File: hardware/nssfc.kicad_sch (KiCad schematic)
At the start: 0 parts

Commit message: made the schematic
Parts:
- added C1, C2: 2.2u, symbol Device:C
- added C10: 1u, symbol Device:C_Small
- added C11: 4.7u, symbol Device:C
- added C12, C5, C6, C7, C8, C9: 100n, symbol Device:C_Small
- added C3, C4: 15p, symbol Device:C_Small
- added R1: 10k, symbol Device:R_Small_US
- added TP1, TP2: TestPoint, symbol Connector:TestPoint
- added U1: STM32F405RGTx, Package_QFP:LQFP-64_10x10mm_P0.5mm, symbol MCU_ST_STM32F4:STM32F405RGTx
- added U2: W25Q128JVP, Package_SON:WSON-8-1EP_6x5mm_P1.27mm_EP3.4x4.3mm, symbol Memory_Flash:W25Q128JVP
- added U3: QMC5883P, nssfc:LGA-16_3x3_Pitch0.5mm_QMC5883P, symbol nssfc:QMC5883P
- added U4: ICM-20602, Package_LGA:LGA-16_3x3mm_P0.5mm_LayoutBorder3x5y, symbol Sensor_Motion:ICM-20602
- added U5: BMP580, Package_LGA:ST_HLGA-10_2x2mm_P0.5mm_LayoutBorder3x2y, symbol nssfc:BMP580
- added Y1: 25MHz, symbol Device:Crystal_GND24
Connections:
- new net: C2.1, U1.31 (VCAP_1)
- new net: C1.1, U1.47 (VCAP_2)
- new net: C11.1, U3.10 (C1)
- new net: U5.3 (VSS), U5.8 (VSS), U5.9 (VSS)
- new net: U3.12 (NC), U3.13 (NC), U3.14 (NC), U3.15 (NC), U3.3 (NC), U3.4 (NC), U3.5 (NC), U3.6 (NC), U3.7 (NC), U3.8 (NC)
- new net +3V3: C10.1, C12.1, C5.1, C6.1, C7.1, C8.1, C9.1, R1.1, U1.1 (VBAT), U1.13 (VDDA), U1.19 (VDD), U1.32 (VDD), U1.48 (VDD), U1.64 (VDD), U2.8 (VCC)
- new net F_SPI_CLK: U2.6 (CLK)
- new net F_SPI_MISO: U2.2 (DO/IO_{1})
- new net F_SPI_MOSI: U2.5 (DI/IO_{0})
- new net GND: C1.2, C10.2, C11.2, C12.2, C2.2, C3.2, C4.2, C5.2, C6.2, C7.2, C8.2, C9.2, TP1.1, U1.12 (VSSA), U1.18 (VSS), U1.63 (VSS), U2.4 (GND), U2.9 (EP), U3.11 (GND), U3.9 (GND), U4.10 (GND), U4.11 (GND), U4.12 (GND), U4.13 (GND), U4.15 (GND), U4.9 (GND), Y1.2 (G), Y1.4 (G)
- new net M_SCK: U3.1 (SCK)
- new net M_SDA: U3.16 (SDA)
- new net NRST: R1.2, TP2.1, U1.7 (NRST)
- new net PH0: C3.1, U1.5 (PH0), Y1.1
- new net PH1: C4.1, U1.6 (PH1), Y1.3
- new net ~{F_SPI_CS}: U2.1 (~{CS})
- new net ~{F_SPI_RST}: U2.7 (~{HOLD}/~{RESET}/IO_{3})
- new net ~{F_SPI_WP}: U2.3 (~{WP}/IO_{2})
- no-connect marks 0 -> 1
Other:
- note added: "15pF capacitance taken assuming 10pF crystal load capacitance and 2.5pF stray capacitance."
- note added: "Barometer"
- note added: "Crystal"
- note added: "Flash"
- note added: "IMU"
- note added: "Magnetometer"
- note added: "add appropriate power converters"
- note added: "button to be added here"
- note added: "ensure ESR<200m (thus no 0402)"
- note added: "qSPI mode not used because stm32f405 does not support it."
- note added: "use SPI with the IMU"

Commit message: saving the repository
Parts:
- added C13, C14: 100n, symbol Device:C_Small
- added C15, C16: .1u, symbol Device:C_Small
- added C17: 2.2u, symbol Device:C_Small
- added C18: 10n, symbol Device:C_Small
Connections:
- net +3V3: now also U4.16 (VDD), C16.1, C17.1
- net GND: now also U5.3 (VSS), U5.8 (VSS), U5.9 (VSS), C13.1, C14.1, C15.2, C16.2, C17.2, C18.1
- net BMP_SPI_MISO: now reaches U1.10 (PC2)
- net BMP_SPI_MISO: now also U5.5 (SDO)
- net BMP_SPI_MOSI: now reaches U1.11 (PC3)
- net BMP_SPI_MOSI: now also U5.4 (SDI)
- net IMU_SPI_CS: now reaches U1.20 (PA4)
- net IMU_SPI_CS: now also U4.5 (~{CS})
- net IMU_SPI_SCK: now reaches U1.21 (PA5)
- net IMU_SPI_SCK: now also U4.2 (SCL/SPC)
- net IMU_SPI_MISO: now reaches U1.22 (PA6)
- net IMU_SPI_MISO: now also U4.4 (SAO/SD0)
- net IMU_SPI_MOSI: now reaches U1.23 (PA7)
- net IMU_SPI_MOSI: now also U4.3 (SDA/SDI)
- net BMP_SPI_SCK: now reaches U1.29 (PB10)
- net BMP_SPI_SCK: now also U5.2 (SCK)
- net BMP_SPI_CSB: now reaches U1.33 (PB12)
- net BMP_SPI_CSB: now also U5.6 (CSB)
- net at U5.1 (VDDIO): now also C13.2
- net at U5.10 (VDD): now also C14.2
- net at U4.1 (VDDIO): now also C18.2
- net at U4.14 (REGOUT): now also C15.1
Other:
- moved on the sheet: U4

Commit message: worked on the schematic
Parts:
- added C19, C23, C25: 100n, Capacitor_SMD:C_0402_1005Metric, symbol Device:C_Small
- added C20: 22u, Capacitor_SMD:C_0805_2012Metric, symbol Device:C
- added C21, C22, C24: 10u, Capacitor_SMD:C_0805_2012Metric, symbol Device:C
- added D1, D2: D_Schottky, Diode_SMD:D_SOD-123F, symbol Device:D_Schottky_Small
- added J1: USB_C_Receptacle_USB2.0_16P, Connector_USB:USB_C_Receptacle_XKB_U262-16XN-4BVC11, symbol Connector:USB_C_Receptacle_USB2.0_16P
- added L1: 4.7u, Inductor_SMD:L_Changjiang_FNR4020S, symbol Device:L
- added R2, R3: 4.7k, Resistor_SMD:R_0402_1005Metric, symbol Device:R_Small_US
- added R4, R5: 5.1k, Resistor_SMD:R_0402_1005Metric, symbol Device:R_Small_US
- added R6: 10k, Resistor_SMD:R_0402_1005Metric, symbol Device:R_Small_US
- added SW1: SW_Push, Button_Switch_SMD:SW_SPST_PTS810, symbol Switch:SW_Push
- added U6: AP63205WU, Package_TO_SOT_SMD:TSOT-23-6, symbol Regulator_Switching:AP63205WU
- added U7: TLV75733PDBV, Package_TO_SOT_SMD:SOT-23-5, symbol Regulator_Linear:TLV75733PDBV
- C1, C10, C12, C13, C14, C18, C2, C3, C4, C5, C6, C7, C8, C9: footprint (none) -> Capacitor_SMD:C_0402_1005Metric
- C11: footprint (none) -> Capacitor_SMD:C_0805_2012Metric
- C15: value .1u -> 100n; footprint (none) -> Capacitor_SMD:C_0402_1005Metric
- C16: value .1u -> 2.2u; footprint (none) -> Capacitor_SMD:C_0402_1005Metric
- C17: value 2.2u -> 100n; footprint (none) -> Capacitor_SMD:C_0402_1005Metric
- R1: footprint (none) -> Resistor_SMD:R_0402_1005Metric
- TP1, TP2: footprint (none) -> TestPoint:TestPoint_Pad_1.0x1.0mm
- Y1: footprint (none) -> Crystal:Crystal_SMD_3225-4Pin_3.2x2.5mm
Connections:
- net +3V3: now also C13.1, C14.1, C18.1, U3.2 (VDD), U4.1 (VDDIO), U5.1 (VDDIO), U5.10 (VDD), C24.1, C25.1, R2.1, R3.1, SW1.1, U7.5 (OUT)
- net BMP_SPI_MISO: now also U1.35 (PB14); no longer U1.10 (PC2)
- net BMP_SPI_MOSI: now also U1.36 (PB15); no longer U1.11 (PC3)
- net BMP_SPI_SCK: now also U1.34 (PB13); no longer U1.29 (PB10)
- net F_SPI_CLK: now also U1.51 (PC10)
- net F_SPI_MISO: now also U1.52 (PC11)
- net F_SPI_MOSI: now also U1.53 (PC12)
- net GND: now also C13.2, C14.2, C18.2, C20.2, C21.2, C22.2, C23.2, C24.2, C25.2, J1.A1 (GND), J1.A12 (GND), J1.B1 (GND), J1.B12 (GND), J1.SH (SHIELD), R4.2, R5.2, R6.2, U6.4 (GND), U7.2 (GND); no longer C13.1, C14.1, C18.1
- net M_SCK: now also U1.59 (PB7), R3.2
- net M_SDA: now also U1.58 (PB6), R2.2
- net ~{F_SPI_CS}: now also U1.50 (PA15)
- net ~{F_SPI_RST}: now also U1.49 (PA14)
- net ~{F_SPI_WP}: now also U1.46 (PA13)
- net IMU_SPI_INT: now reaches U1.17 (PA3)
- net IMU_SPI_INT: now also U4.6 (INT)
- net BMP_SPI_INT: now reaches U1.30 (PB11)
- net BMP_SPI_INT: now also U5.7 (INT)
- net USB_DN: now reaches U1.44 (PA11)
- net USB_DN: now also J1.A7 (D-), J1.B7 (D-)
- net USB_DP: now reaches U1.45 (PA12)
- net USB_DP: now also J1.A6 (D+), J1.B6 (D+)
- net at U1.60 (BOOT0): now also R6.1, SW1.2
- new net: D1.2 (A), J1.A4 (VBUS), J1.A9 (VBUS), J1.B4 (VBUS), J1.B9 (VBUS)
- new net: J1.A5 (CC1), R5.1
- new net: J1.B5 (CC2), R4.1
- new net: C20.1, D2.2 (A), L1.2, U6.1 (FB)
- new net: C19.1, L1.1, U6.5 (SW)
- new net: C19.2, U6.6 (BST)
- new net +5V: C22.1, C23.1, D1.1 (K), D2.1 (K), U7.1 (IN), U7.3 (EN)
- new net VBUS: C21.1, U6.2 (EN), U6.3 (IN)
- no-connect marks 1 -> 3
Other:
- note added: "V_batt to 5v"
- note added: "add 9v buck boost"
- note added: "add power LEDs add connection pads add UARTS and I2C and SBUS controls"
- note added: "buck converter"
- note added: "main LDO"
- note removed: "add appropriate power converters"
- note removed: "button to be added here"
- moved on the sheet: C1, C10, C11, C12, C15, C2, C3, C4, C5, C6, C7, C8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

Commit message: worked on PCB layout
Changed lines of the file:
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@@
+	)
+	(junction
+		(at 213.36 102.87)
+		(diameter 0)
+		(color 0 0 0 0)
+	)
+	(junction
+		(at 261.62 49.53)
+		(diameter 0)
+		(color 0 0 0 0)
+	)
+	(junction
+		(at 276.86 49.53)
+		(diameter 0)
+		(color 0 0 0 0)
+	)
+	(junction
+		(at 236.22 50.8)
+		(diameter 0)
+		(color 0 0 0 0)
+	)
+	(junction
+		(at 82.55 116.84)
+		(diameter 0)
+		(color 0 0 0 0)
+	)
+	(junction
+		(at 212.09 184.15)
+		(diameter 0)
+		(color 0 0 0 0)
+	)
+	(junction
+		(at 60.96 113.03)
+		(diameter 0)
+		(color 0 0 0 0)
+	)
+	(junction
+		(at 269.24 134.62)
+		(diameter 0)
+		(color 0 0 0 0)
+	)
+	(junction
+		(at 62.23 85.09)
+		(diameter 0)
+		(color 0 0 0 0)
+	)
+	(junction
+		(at 201.93 50.8)
+		(diameter 0)
+		(color 0 0 0 0)
+	)
+	(junction
+		(at 168.91 49.53)
+		(diameter 0)
+		(color 0 0 0 0)
+	)
+	(junction
+		(at 146.05 128.27)
+		(diameter 0)
+		(color 0 0 0 0)
+	)
+	(junction
+		(at 161.29 49.53)
+		(diameter 0)
+		(color 0 0 0 0)
+	)
+	(junction
+		(at 180.34 115.57)
+		(diameter 0)
+		(color 0 0 0 0)
 	)
 	(junction
@@
 	)
 	(junction
-		(at 213.36 102.87)
-		(diameter 0)
-		(color 0 0 0 0)
-	)
-	(junction
-		(at 261.62 49.53)
-		(diameter 0)
-		(color 0 0 0 0)
-	)
-	(junction
-		(at 276.86 49.53)
-		(diameter 0)
-		(color 0 0 0 0)
-	)
-	(junction
-		(at 236.22 50.8)
-		(diameter 0)
-		(color 0 0 0 0)
-	)
-	(junction
-		(at 82.55 116.84)
-		(diameter 0)
-		(color 0 0 0 0)
-	)
-	(junction
-		(at 60.96 113.03)
-		(diameter 0)
-		(color 0 0 0 0)
-	)
-	(junction
-		(at 269.24 134.62)
-		(diameter 0)
-		(color 0 0 0 0)
-	)
-	(junction
-		(at 62.23 85.09)
-		(diameter 0)
-		(color 0 0 0 0)
-	)
-	(junction
-		(at 201.93 50.8)
-		(diameter 0)
-		(color 0 0 0 0)
-	)
-	(junction
-		(at 168.91 49.53)
-		(diameter 0)
-		(color 0 0 0 0)
-	)
-	(junction
-		(at 146.05 128.27)
-		(diameter 0)
-		(color 0 0 0 0)
-	)
-	(junction
-		(at 161.29 49.53)
-		(diameter 0)
-		(color 0 0 0 0)
-	)
-	(junction
-		(at 180.34 115.57)
-		(diameter 0)
-		(color 0 0 0 0)
-	)
-	(junction
 		(at 81.28 64.77)
 		(diameter 0)
@@
 	(junction
 		(at 217.17 175.26)
-		(diameter 0)
-		(color 0 0 0 0)
-	)
-	(junction
-		(at 212.09 184.15)
 		(diameter 0)
 		(color 0 0 0 0)
@@
 	(wire
 		(pts
-			(xy 212.09 184.15) (xy 232.41 184.15)
+			(xy 212.09 184.15) (xy 234.95 184.15)
 		)
 		(stroke
@@
 	(wire
 		(pts
-			(xy 222.25 181.61) (xy 232.41 181.61)
+			(xy 222.25 181.61) (xy 234.95 181.61)
 		)
 		(stroke
@@
 	)
 	(label "M_SCK"
-		(at 232.41 184.15 180)
+		(at 234.95 184.15 180)
 		(effects
 			(font
@@
 	)
 	(label "M_SDA"
-		(at 232.41 181.61 180)
+		(at 234.95 181.61 180)
 		(effects
 			(font

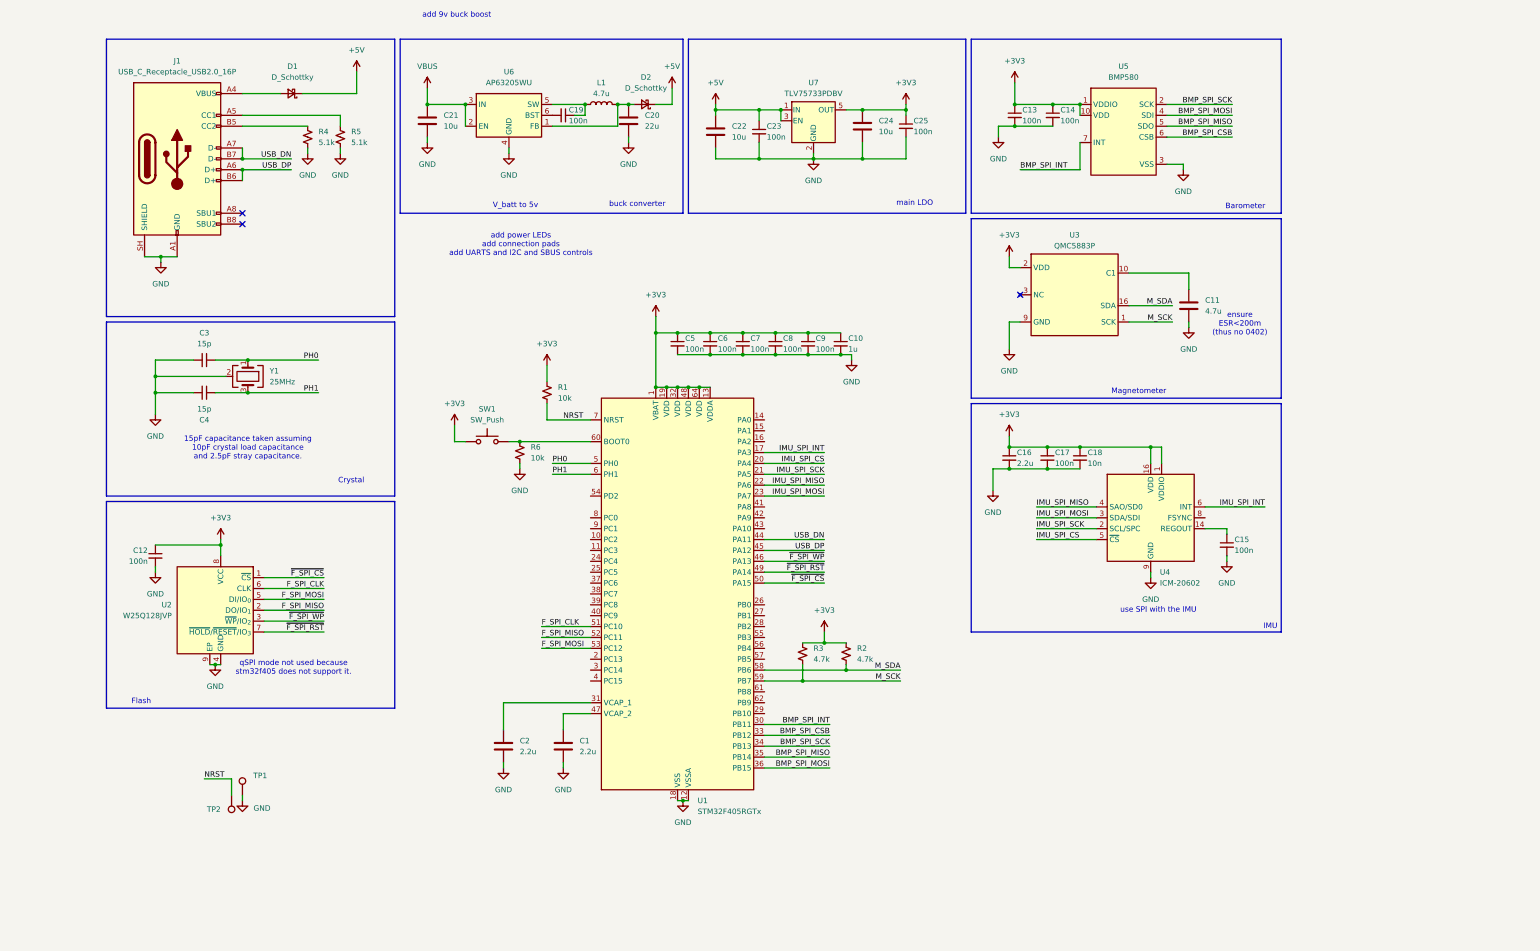
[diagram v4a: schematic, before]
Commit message: layout change in PCB
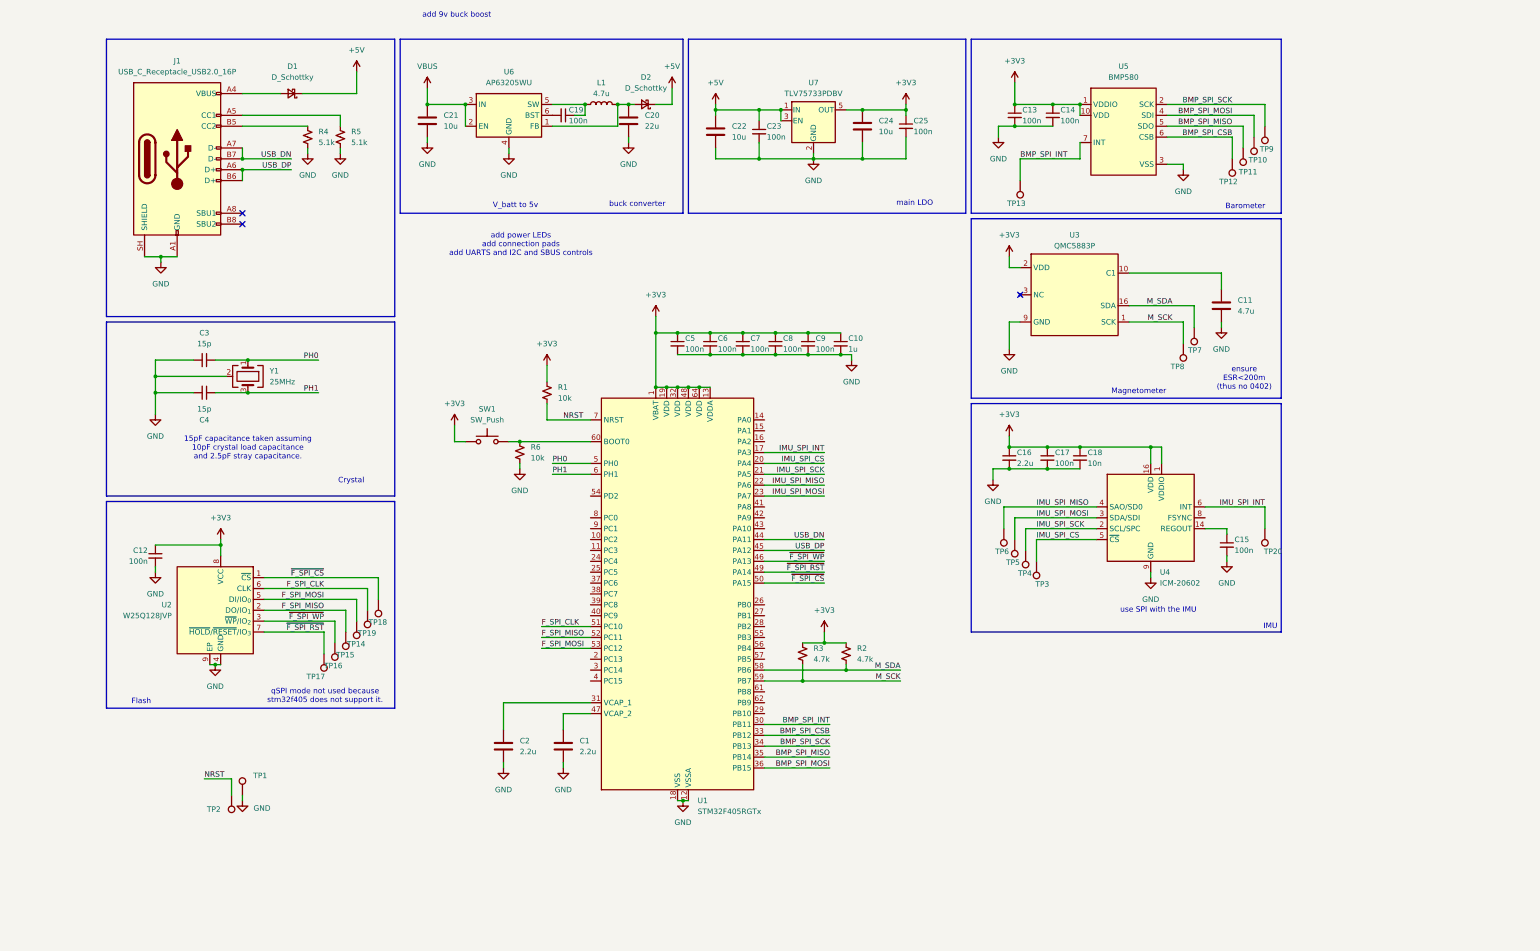
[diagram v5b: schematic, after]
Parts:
- added TP10, TP11, TP12, TP13, TP14, TP15, TP16, TP17, TP18, TP19, TP20, TP3, TP4, TP5, TP6, TP7, TP8, TP9: TestPoint, TestPoint:TestPoint_Pad_1.5x1.5mm, symbol Connector:TestPoint
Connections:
- net BMP_SPI_CSB: now also TP12.1
- net BMP_SPI_INT: now also TP13.1
- net BMP_SPI_MISO: now also TP11.1
- net BMP_SPI_MOSI: now also TP10.1
- net BMP_SPI_SCK: now also TP9.1
- net F_SPI_CLK: now also TP19.1
- net F_SPI_MISO: now also TP15.1
- net F_SPI_MOSI: now also TP14.1
- net IMU_SPI_CS: now also TP3.1
- net IMU_SPI_INT: now also TP20.1
- net IMU_SPI_MISO: now also TP6.1
- net IMU_SPI_MOSI: now also TP5.1
- net IMU_SPI_SCK: now also TP4.1
- net M_SCK: now also TP8.1
- net M_SDA: now also TP7.1
- net ~{F_SPI_CS}: now also TP18.1
- net ~{F_SPI_RST}: now also TP17.1
- net ~{F_SPI_WP}: now also TP16.1
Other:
- moved on the sheet: C11

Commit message: placement session: i am locked in
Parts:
- added D3, D4, D5: LED, LED_SMD:LED_0402_1005Metric, symbol Device:LED
- added R7: 1k, Resistor_SMD:R_0402_1005Metric, symbol Device:R_Small_US
- added R8: 220, Resistor_SMD:R_0402_1005Metric, symbol Device:R_Small_US
- added R9: 100, Resistor_SMD:R_0402_1005Metric, symbol Device:R_Small_US
- added TP21, TP22, TP23, TP24, TP25, TP26, TP27, TP28, TP29, TP30, TP31, TP32, TP33, TP34, TP35, TP36, TP37, TP38, TP39, TP40, TP41, TP42, TP43, TP44, TP45, TP46, TP47, TP48, TP49: TestPoint, nssfc:PAD_1.5mm, symbol Connector:TestPoint
- added TP50, TP51: TestPoint, TestPoint:TestPoint_Pad_3.0x3.0mm, symbol Connector:TestPoint
- TP10, TP11, TP12, TP13, TP14, TP15, TP16, TP17, TP18, TP19, TP20, TP3, TP4, TP5, TP6, TP7, TP8, TP9: footprint TestPoint:TestPoint_Pad_1.5x1.5mm -> nssfc:PAD_1.5mm
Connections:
- net +3V3: now also D5.2 (A)
- net +5V: now also D4.2 (A)
- net GND: now also R7.2, R8.2, R9.2, TP51.1
- net VBUS: now also D3.2 (A), TP50.1
- net at U1.10 (PC2): now also TP23.1
- net at U1.11 (PC3): now also TP24.1
- net at U1.14 (PA0): now also TP35.1
- net at U1.15 (PA1): now also TP36.1
- net at U1.16 (PA2): now also TP37.1
- net at U1.2 (PC13): now also TP31.1
- net at U1.24 (PC4): now also TP25.1
- net at U1.25 (PC5): now also TP26.1
- net at U1.26 (PB0): now also TP41.1
- net at U1.27 (PB1): now also TP42.1
- net at U1.28 (PB2): now also TP43.1
- net at U1.29 (PB10): now also TP49.1
- net at U1.3 (PC14): now also TP32.1
- net at U1.37 (PC6): now also TP27.1
- net at U1.38 (PC7): now also TP28.1
- net at U1.39 (PC8): now also TP29.1
- net at U1.4 (PC15): now also TP33.1
- net at U1.40 (PC9): now also TP30.1
- net at U1.41 (PA8): now also TP38.1
- net at U1.42 (PA9): now also TP39.1
- net at U1.43 (PA10): now also TP40.1
- net at U1.54 (PD2): now also TP34.1
- net at U1.55 (PB3): now also TP44.1
- net at U1.56 (PB4): now also TP45.1
- net at U1.57 (PB5): now also TP46.1
- net at U1.61 (PB8): now also TP47.1
- net at U1.62 (PB9): now also TP48.1
- net at U1.8 (PC0): now also TP21.1
- net at U1.9 (PC1): now also TP22.1
- new net: D4.1 (K), R8.1
- new net: D5.1 (K), R9.1
- new net: D3.1 (K), R7.1
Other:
- moved on the sheet: R2, R3, TP1, TP2

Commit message: completed placement
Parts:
- removed C18: 10n, Capacitor_SMD:C_0402_1005Metric, symbol Device:C_Small
- removed TP10, TP11, TP12, TP13, TP14, TP15, TP16, TP17, TP18, TP19, TP20, TP3, TP4, TP5, TP6, TP7, TP8, TP9: TestPoint, nssfc:PAD_1.5mm, symbol Connector:TestPoint
- added TP52, TP53, TP55, TP58, TP59, TP60, TP61, TP62, TP63, TP64: TestPoint, nssfc:PAD_1.5mm, symbol Connector:TestPoint
- TP50, TP51: footprint TestPoint:TestPoint_Pad_3.0x3.0mm -> TestPoint:TestPoint_Pad_2.0x2.0mm
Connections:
- net +3V3: now also TP52.1, TP53.1, TP55.1
- net +5V: now also TP62.1, TP63.1
- net GND: now also TP58.1, TP59.1, TP60.1, TP61.1, TP64.1
- no-connect marks 3 -> 4

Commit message: done PCB
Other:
- note removed: "add 9v buck boost"
- note removed: "add power LEDs add connection pads add UARTS and I2C and SBUS controls"
- moved on the sheet: C1, C10, C11, C12, C13, C14, C15, C16, C17, C19, C2, C20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
